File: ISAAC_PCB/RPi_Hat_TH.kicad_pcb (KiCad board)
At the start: 2 copper layers, 65 x 56 mm, 5 parts, among them J2 RPi_GPIO

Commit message: Updated Everything Again!
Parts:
- added C1: CP1_Small, Capacitor_THT:CP_Radial_D4.0mm_P1.50mm, F.Cu at (292.9, 74.2)
- added C2: C_Small, Capacitor_THT:CP_Radial_D4.0mm_P1.50mm, F.Cu at (277.0, 92.7)
- added D1: DIODE, Diode_SMD:D_1812_4532Metric_Pad1.30x3.40mm_HandSolder, F.Cu at (278.6, 87.4)
- added D10: DIODE, Diode_SMD:D_1812_4532Metric_Pad1.30x3.40mm_HandSolder, F.Cu at (288.9, 68.9)
- added D11: DIODE, Diode_SMD:D_1812_4532Metric_Pad1.30x3.40mm_HandSolder, F.Cu at (271.3, 88.8)
- added D12: DIODE, Diode_SMD:D_1812_4532Metric_Pad1.30x3.40mm_HandSolder, F.Cu at (298.7, 60.9)
- added D13: DIODE, Diode_SMD:D_1812_4532Metric_Pad1.30x3.40mm_HandSolder, F.Cu at (279.8, 81.9)
- added D14: DIODE, Diode_SMD:D_1812_4532Metric_Pad1.30x3.40mm_HandSolder, F.Cu at (287.2, 76.8)
- added D15: DIODE, Diode_SMD:D_1812_4532Metric_Pad1.30x3.40mm_HandSolder, F.Cu at (269.5, 93.9)
- added D16: DIODE, Diode_SMD:D_1812_4532Metric_Pad1.30x3.40mm_HandSolder, F.Cu at (298.1, 65.9)
- added D2: DIODE, Diode_SMD:D_1812_4532Metric_Pad1.30x3.40mm_HandSolder, F.Cu at (287.2, 81.9)
- added D3: DIODE, Diode_SMD:D_1812_4532Metric_Pad1.30x3.40mm_HandSolder, F.Cu at (254.8, 95.2)
- added D4: DIODE, Diode_SMD:D_1812_4532Metric_Pad1.30x3.40mm_HandSolder, F.Cu at (263.9, 88.8)
- added D5: DIODE, Diode_SMD:D_1812_4532Metric_Pad1.30x3.40mm_HandSolder, F.Cu at (290.8, 63.8)
- added D6: DIODE, Diode_SMD:D_1812_4532Metric_Pad1.30x3.40mm_HandSolder, F.Cu at (271.9, 82.3)
- added D7: DIODE, Diode_SMD:D_1812_4532Metric_Pad1.30x3.40mm_HandSolder, F.Cu at (298.7, 55.9)
- added D8: DIODE, Diode_SMD:D_1812_4532Metric_Pad1.30x3.40mm_HandSolder, F.Cu at (279.8, 76.8)
- added D9: DIODE, Diode_SMD:D_1812_4532Metric_Pad1.30x3.40mm_HandSolder, F.Cu at (262.2, 95.2)
- added H1: MountingHole, MountingHole:MountingHole_3.2mm_M3, F.Cu at (291.1, 57.3)
- added H2: MountingHole, MountingHole:MountingHole_3.2mm_M3, F.Cu at (272.2, 75.8)
- added H3: MountingHole, MountingHole:MountingHole_3.2mm_M3, F.Cu at (281.3, 70.3)
- added H4: MountingHole, MountingHole:MountingHole_3.2mm_M3, F.Cu at (264.2, 82.3)
- added J1: Conn_02x04_Top_Bottom, Connector_Molex:Molex_Mini-Fit_Jr_5569-08A2_2x04_P4.20mm_Horizontal, F.Cu at (225.7, 91.6)
- added J3: Screw_Terminal_01x02, footprints:TE_282837-2, F.Cu at (247.9, 81.3)
- added J4: XT60PW-M, footprints:AMASS_XT60PW-M, F.Cu at (250.6, 64.5)
- added J5: Raspberry_Pi_2_3, footprints:Pin_Header_Straight_2x20, F.Cu at (147.6, 68.8)
- added R1: 10K, Resistor_SMD:R_0805_2012Metric_Pad1.20x1.40mm_HandSolder, F.Cu at (282.9, 91.8)
- added R10: 10K, Resistor_SMD:R_0805_2012Metric_Pad1.20x1.40mm_HandSolder, F.Cu at (256.1, 80.9)
- added R11: 10K, Resistor_SMD:R_0805_2012Metric_Pad1.20x1.40mm_HandSolder, F.Cu at (256.1, 83.8)
- added R12: 10K, Resistor_SMD:R_0805_2012Metric_Pad1.20x1.40mm_HandSolder, F.Cu at (268.2, 97.9)
- added R13: 10K, Resistor_SMD:R_0805_2012Metric_Pad1.20x1.40mm_HandSolder, F.Cu at (284.6, 85.9)
- added R14: 10K, Resistor_SMD:R_0805_2012Metric_Pad1.20x1.40mm_HandSolder, F.Cu at (272.9, 97.9)
- added R15: 10K, Resistor_SMD:R_0805_2012Metric_Pad1.20x1.40mm_HandSolder, F.Cu at (298.8, 69.9)
- added R16: 10K, Resistor_SMD:R_0805_2012Metric_Pad1.20x1.40mm_HandSolder, F.Cu at (298.8, 72.9)
- added R2: 10K, Resistor_SMD:R_0805_2012Metric_Pad1.20x1.40mm_HandSolder, F.Cu at (289.4, 88.8)
- added R3: 10K, Resistor_SMD:R_0805_2012Metric_Pad1.20x1.40mm_HandSolder, F.Cu at (298.8, 75.8)
- added R4: 10K, Resistor_SMD:R_0805_2012Metric_Pad1.20x1.40mm_HandSolder, F.Cu at (293.2, 81.4)
- added R5: 10K, Resistor_SMD:R_0805_2012Metric_Pad1.20x1.40mm_HandSolder, F.Cu at (289.4, 85.9)
- added R6: 10K, Resistor_SMD:R_0805_2012Metric_Pad1.20x1.40mm_HandSolder, F.Cu at (284.6, 88.8)
- added R7: 10K, Resistor_SMD:R_0805_2012Metric_Pad1.20x1.40mm_HandSolder, F.Cu at (293.2, 78.4)
- added R8: 10K, Resistor_SMD:R_0805_2012Metric_Pad1.20x1.40mm_HandSolder, F.Cu at (277.7, 96.9)
- added R9: 10K, Resistor_SMD:R_0805_2012Metric_Pad1.20x1.40mm_HandSolder, F.Cu at (256.1, 77.9)
- added U10: DMN4026SSD, footprints:SOIC127P600X150-8N, F.Cu at (264.0, 68.6)
- added U11: MC7905BD2TR4G, footprints:TO254P1524X483-3, F.Cu at (268.9, 59.4)
- added U2: DMN4026SSD, footprints:SOIC127P600X150-8N, F.Cu at (247.0, 96.0)
- added U3: DMN4026SSD, footprints:SOIC127P600X150-8N, F.Cu at (256.0, 89.5)
- added U4: DMN4026SSD, footprints:SOIC127P600X150-8N, F.Cu at (282.9, 63.1)
- added U5: DMN4026SSD, footprints:SOIC127P600X150-8N, F.Cu at (273.1, 68.6)
- added U7: DMN4026SSD, footprints:SOIC127P600X150-8N, F.Cu at (247.0, 89.5)
- added U8: DMN4026SSD, footprints:SOIC127P600X150-8N, F.Cu at (264.0, 75.1)
- added U9: DMN4026SSD, footprints:SOIC127P600X150-8N, F.Cu at (282.9, 56.6)
- J2: value RPi_GPIO -> Conn_02x04_Top_Bottom; footprint RPi_Hat:Pin_Header_Straight_2x20 -> Connector_Molex:Molex_Mini-Fit_Jr_5569-08A2_2x04_P4.20mm_Horizontal
- moved J2 78.2 mm to (225.7, 68.3), turned to 0 degrees
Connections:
- J2 pad 1: Net-(J2-Pad1) -> SOL1
- J2 pad 2: Net-(J2-Pad2) -> SOL2
- J2 pad 3: Net-(J2-Pad3) -> SOL3
- J2 pad 4: Net-(J2-Pad4) -> SOL4
- J2 pad 5: Net-(J2-Pad5) -> SOL5
- J2 pad 6: Net-(J2-Pad6) -> SOL6
- J2 pad 7: Net-(J2-Pad7) -> SOL7
- J2 pad 8: Net-(J2-Pad8) -> SOL8

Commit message: Updated PCB and Tracing
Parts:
- removed H1, H2, H3, H4: MountingHole, MountingHole:MountingHole_3.2mm_M3
- added U6: module_mpu6050, usini_sensors:module_mpu6050, F.Cu at (140.5, 101.9)
- moved R3 176.6 mm to (122.4, 85.3), turned to 270 degrees
- moved D12 172.3 mm to (130.4, 97.3), turned to 180 degrees
- moved R2 170.0 mm to (119.4, 85.3), turned to 270 degrees
- moved R4 168.0 mm to (125.2, 85.3), turned to 270 degrees
- moved R1 166.7 mm to (116.3, 85.3), turned to 270 degrees
- moved R15 165.8 mm to (134.4, 91.4), turned to 270 degrees
- moved D16 165.2 mm to (136.4, 99.6), turned to 270 degrees
- moved R16 162.4 mm to (137.4, 91.4), turned to 270 degrees
- moved R5 161.1 mm to (128.3, 85.3), turned to 270 degrees
- moved D14 159.5 mm to (130.4, 105.9), turned to 180 degrees
- moved R7 159.0 mm to (134.4, 85.3), turned to 270 degrees
- moved R13 156.5 mm to (128.3, 91.5), turned to 270 degrees
- moved R6 153.4 mm to (131.3, 85.3), turned to 270 degrees
- moved U4 151.0 mm to (132.6, 77.2), turned to 90 degrees
- moved D13 150.8 mm to (130.4, 101.6), turned to 180 degrees
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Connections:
- J3 pad 1: VCC -> GND
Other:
- outline, holes or cut-outs redrawn
- board text added: "+"
- board text added: "-"

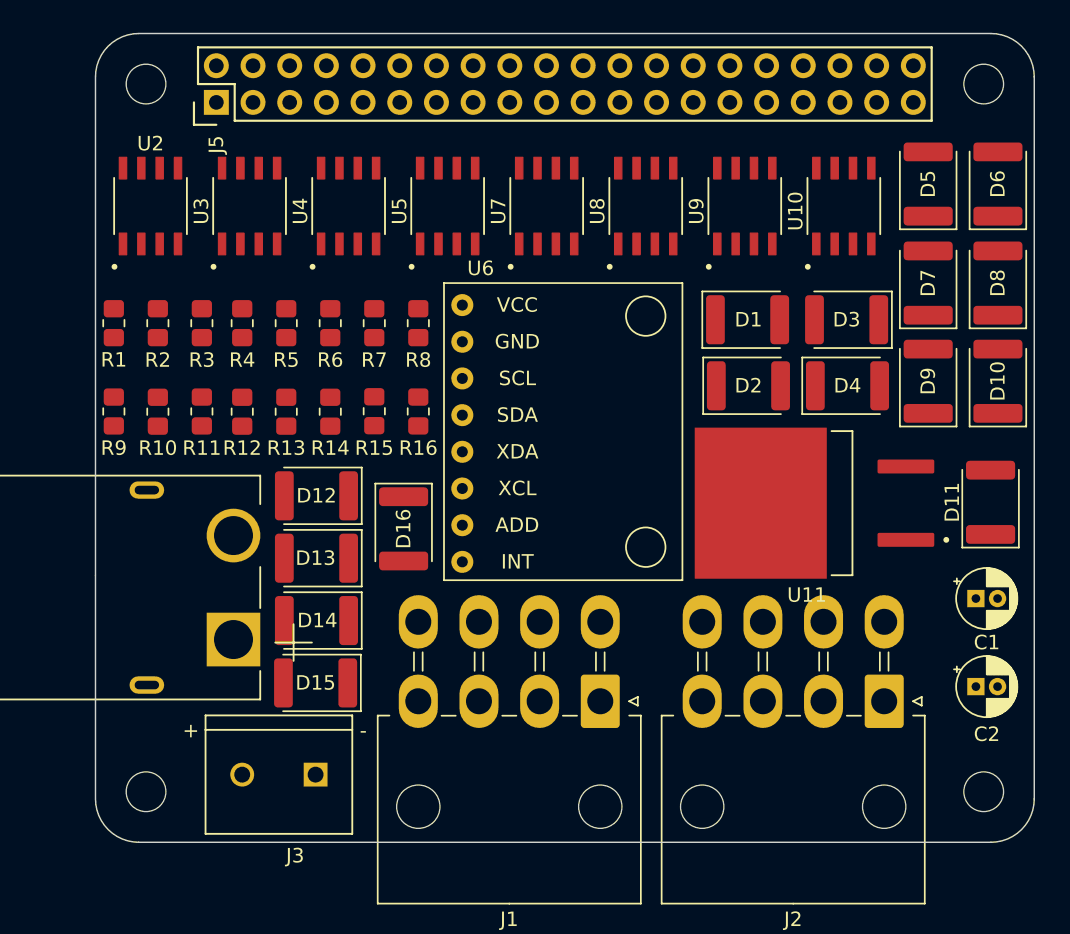
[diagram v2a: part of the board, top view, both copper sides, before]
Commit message: Finished tracing PCB
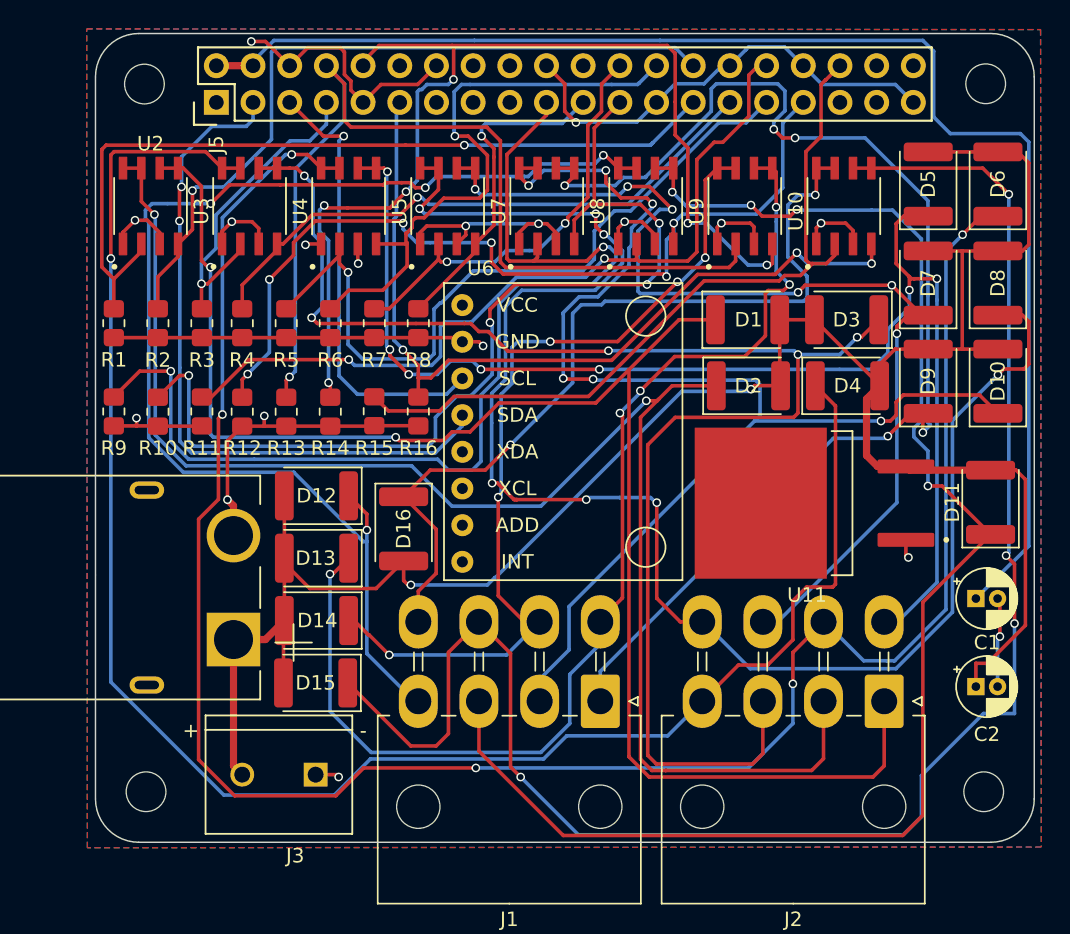
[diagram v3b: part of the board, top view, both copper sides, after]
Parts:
- moved ? 0.14 mm to (176.7, 68.8)
- moved ? 0.11 mm to (118.5, 68.8)
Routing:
- net GND: track 0.00 -> 155.2 mm, vias 0 -> 18
- net VCC: track 0.00 -> 154.0 mm, vias 0 -> 2
- net SOL6: track 0.00 -> 141.2 mm, vias 0 -> 5
- net SOL4: track 0.00 -> 121.4 mm, vias 0 -> 1
- net SOL15: track 0.00 -> 118.5 mm, vias 0 -> 4
- net SOL8: track 0.00 -> 112.6 mm, vias 0 -> 7
- net SOL1: track 0.00 -> 109.4 mm, vias 0 -> 2
- net SOL2: track 0.00 -> 107.2 mm, vias 0 -> 2
- net SOL3: track 0.00 -> 104.6 mm, vias 0 -> 5
- net SOL11: track 0.00 -> 104.0 mm, vias 0 -> 4
- net +5V: track 0.00 -> 95.9 mm
- net SOL5: track 0.00 -> 92.5 mm, vias 0 -> 7
- net SOL10: track 0.00 -> 89.3 mm, vias 0 -> 6
- net SOL9: track 0.00 -> 87.8 mm, vias 0 -> 5
- net SOL12: track 0.00 -> 86.9 mm, vias 0 -> 4
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- added copper zone on B.Cu, net GND
- added copper zone on F.Cu, net GND

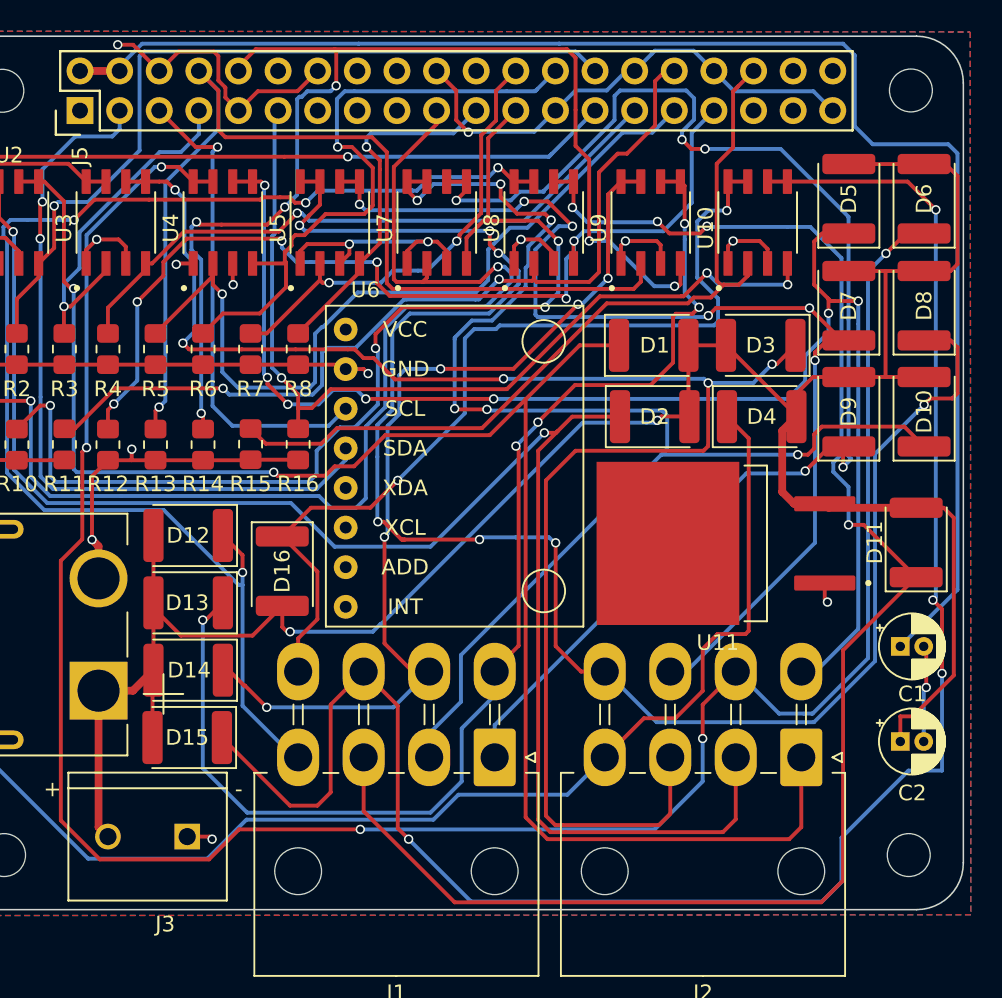
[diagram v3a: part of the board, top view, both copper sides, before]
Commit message: Fixed GND layers
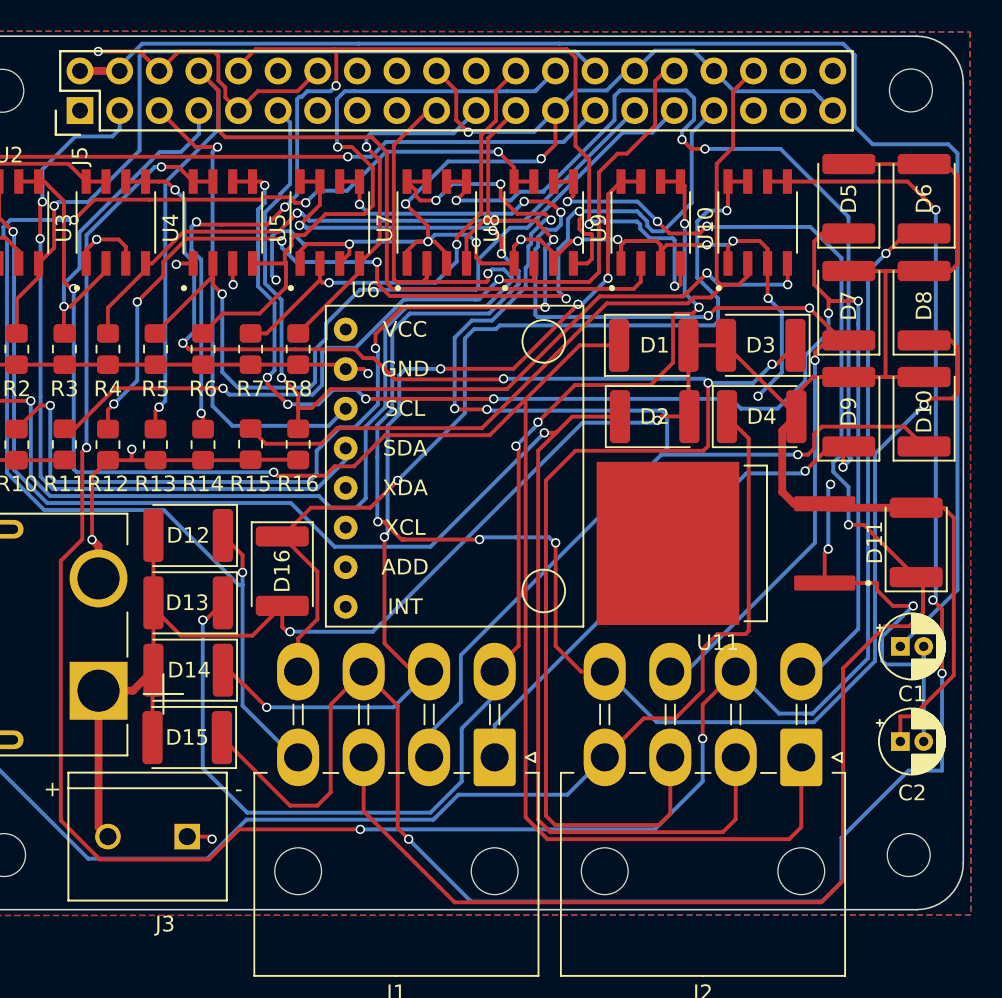
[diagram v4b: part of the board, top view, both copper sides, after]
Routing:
- net GND: track 155.2 -> 228.4 mm, vias 18 -> 27
- net GATE12: track 61.9 -> 68.3 mm
- net SOL11: track 104.0 -> 105.5 mm
- net GATE14: track 75.6 -> 77.0 mm
- net GATE16: track 58.0 -> 59.4 mm
- net SOL12: track 86.9 -> 88.3 mm
- net SOL5: track 92.5 -> 93.7 mm
- net GATE7: track 29.4 -> 30.1 mm
